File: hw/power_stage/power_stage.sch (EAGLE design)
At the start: 47 parts, among them IC1H MIC4420M, IC1L MIC4429M, IC2H MIC4420M, IC2L MIC4429M, J1 AC1, J2 AC2, J3 OUT1, J4 OUT2

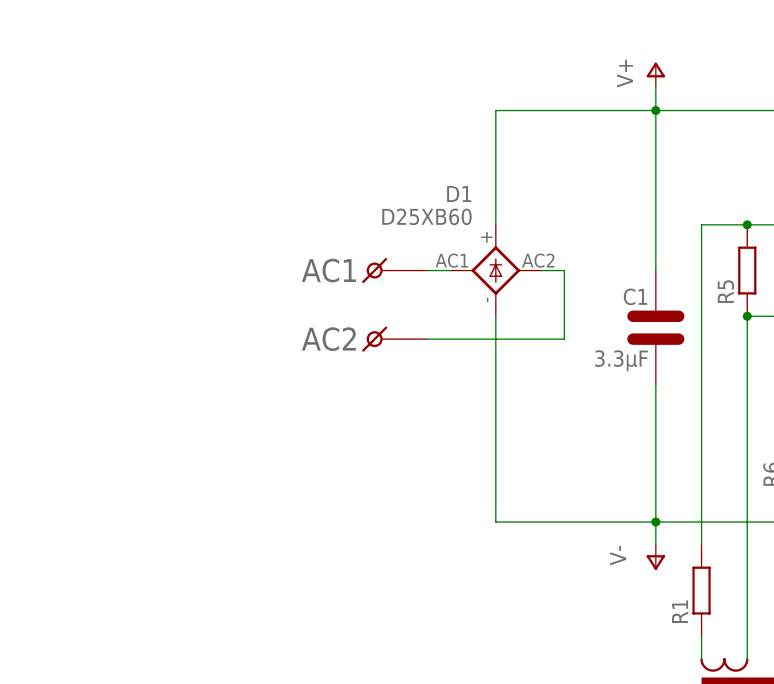
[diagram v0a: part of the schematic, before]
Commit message: Adapted power_stage.brd to be 100x100mm
This enables us to use cheap PCB fab services.
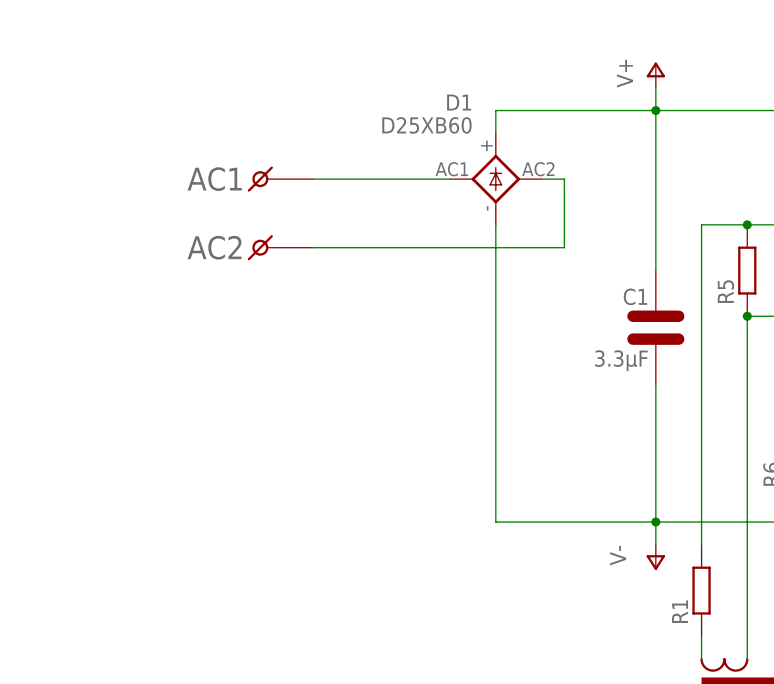
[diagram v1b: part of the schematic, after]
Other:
- moved on the sheet: D1
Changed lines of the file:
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@@
 <layer number="48" name="Document" color="7" fill="1" visible="no" active="no"/>
 <layer number="49" name="Reference" color="7" fill="1" visible="no" active="no"/>
+<layer number="50" name="dxf" color="7" fill="1" visible="no" active="no"/>
 <layer number="51" name="tDocu" color="7" fill="1" visible="no" active="no"/>
 <layer number="52" name="bDocu" color="7" fill="1" visible="no" active="no"/>
+<layer number="53" name="tGND_GNDA" color="7" fill="9" visible="no" active="no"/>
+<layer number="54" name="bGND_GNDA" color="1" fill="9" visible="no" active="no"/>
+<layer number="56" name="wert" color="7" fill="1" visible="no" active="no"/>
 <layer number="90" name="Modules" color="5" fill="1" visible="yes" active="yes"/>
 <layer number="91" name="Nets" color="2" fill="1" visible="yes" active="yes"/>
@@
 <layer number="98" name="Guide" color="6" fill="1" visible="yes" active="yes"/>
 <layer number="99" name="SpiceOrder" color="5" fill="1" visible="yes" active="yes"/>
+<layer number="100" name="Muster" color="7" fill="1" visible="no" active="no"/>
+<layer number="101" name="Patch_Top" color="12" fill="4" visible="yes" active="yes"/>
+<layer number="102" name="Vscore" color="7" fill="1" visible="yes" active="yes"/>
+<layer number="103" name="tMap" color="7" fill="1" visible="yes" active="yes"/>
+<layer number="104" name="Name" color="16" fill="1" visible="yes" active="yes"/>
+<layer number="105" name="tPlate" color="7" fill="1" visible="yes" active="yes"/>
+<layer number="106" name="bPlate" color="7" fill="1" visible="yes" active="yes"/>
+<layer number="107" name="Crop" color="7" fill="1" visible="yes" active="yes"/>
+<layer number="108" name="tplace-old" color="10" fill="1" visible="yes" active="yes"/>
+<layer number="109" name="ref-old" color="11" fill="1" visible="yes" active="yes"/>
+<layer number="116" name="Patch_BOT" color="9" fill="4" visible="yes" active="yes"/>
+<layer number="121" name="_tsilk" color="7" fill="1" visible="yes" active="yes"/>
+<layer number="122" name="_bsilk" color="7" fill="1" visible="yes" active="yes"/>
+<layer number="125" name="_tNames" color="7" fill="1" visible="yes" active="yes"/>
+<layer number="144" name="Drill_legend" color="7" fill="1" visible="yes" active="yes"/>
+<layer number="151" name="HeatSink" color="7" fill="1" visible="yes" active="yes"/>
+<layer number="199" name="Contour" color="7" fill="1" visible="yes" active="yes"/>
+<layer number="200" name="200bmp" color="1" fill="10" visible="yes" active="yes"/>
+<layer number="201" name="201bmp" color="2" fill="10" visible="yes" active="yes"/>
+<layer number="202" name="202bmp" color="3" fill="10" visible="yes" active="yes"/>
+<layer number="203" name="203bmp" color="4" fill="10" visible="yes" active="yes"/>
+<layer number="204" name="204bmp" color="5" fill="10" visible="yes" active="yes"/>
+<layer number="205" name="205bmp" color="6" fill="10" visible="yes" active="yes"/>
+<layer number="206" name="206bmp" color="7" fill="10" visible="yes" active="yes"/>
+<layer number="207" name="207bmp" color="8" fill="10" visible="yes" active="yes"/>
+<layer number="208" name="208bmp" color="9" fill="10" visible="yes" active="yes"/>
+<layer number="209" name="209bmp" color="7" fill="1" visible="yes" active="yes"/>
+<layer number="210" name="210bmp" color="7" fill="1" visible="yes" active="yes"/>
+<layer number="211" name="211bmp" color="7" fill="1" visible="yes" active="yes"/>
+<layer number="212" name="212bmp" color="7" fill="1" visible="yes" active="yes"/>
+<layer number="213" name="213bmp" color="7" fill="1" visible="yes" active="yes"/>
+<layer number="214" name="214bmp" color="7" fill="1" visible="yes" active="yes"/>
+<layer number="215" name="215bmp" color="7" fill="1" visible="yes" active="yes"/>
+<layer number="216" name="216bmp" color="7" fill="1" visible="yes" active="yes"/>
+<layer number="217" name="217bmp" color="18" fill="1" visible="no" active="no"/>
+<layer number="218" name="218bmp" color="19" fill="1" visible="no" active="no"/>
+<layer number="219" name="219bmp" color="20" fill="1" visible="no" active="no"/>
+<layer number="220" name="220bmp" color="21" fill="1" visible="no" active="no"/>
+<layer number="221" name="221bmp" color="22" fill="1" visible="no" active="no"/>
+<layer number="222" name="222bmp" color="23" fill="1" visible="no" active="no"/>
+<layer number="223" name="223bmp" color="24" fill="1" visible="no" active="no"/>
+<layer number="224" name="224bmp" color="25" fill="1" visible="no" active="no"/>
+<layer number="250" name="Descript" color="3" fill="1" visible="no" active="no"/>
+<layer number="251" name="SMDround" color="12" fill="11" visible="no" active="no"/>
+<layer number="254" name="cooling" color="7" fill="1" visible="yes" active="yes"/>
 </layers>
 <schematic xreflabel="%F%N/%S.%C%R" xrefpart="/%S.%C%R">
@@
 <attribute name="VALUE" x="-31.242" y="54.61" size="1.778" layer="96" ratio="15" align="top-right"/>
 </instance>
-<instance part="D1" gate="G$1" x="-48.26" y="63.5" smashed="yes" rot="R90">
-<attribute name="NAME" x="-50.8" y="71.12" size="1.778" layer="95" align="bottom-right"/>
-<attribute name="VALUE" x="-50.8" y="68.58" size="1.778" layer="96" align="bottom-right"/>
-</instance>
-<instance part="J1" gate="G$1" x="-60.96" y="63.5" rot="R180"/>
-<instance part="J2" gate="G$1" x="-60.96" y="55.88" rot="R180"/>
+<instance part="D1" gate="G$1" x="-48.26" y="73.66" smashed="yes" rot="R90">
+<attribute name="NAME" x="-50.8" y="81.28" size="1.778" layer="95" align="bottom-right"/>
+<attribute name="VALUE" x="-50.8" y="78.74" size="1.778" layer="96" align="bottom-right"/>
+</instance>
+<instance part="J1" gate="G$1" x="-73.66" y="73.66" rot="R180"/>
+<instance part="J2" gate="G$1" x="-73.66" y="66.04" rot="R180"/>
 <instance part="IGBT1H" gate="G$1" x="-2.54" y="71.12" smashed="yes">
 <attribute name="NAME" x="-5.08" y="69.596" size="1.778" layer="95" align="bottom-right"/>
@@
 <net name="AC2" class="0">
 <segment>
-<wire x1="-40.64" y1="55.88" x2="-40.64" y2="63.5" width="0.1524" layer="91"/>
+<wire x1="-40.64" y1="66.04" x2="-40.64" y2="73.66" width="0.1524" layer="91"/>
 <pinref part="D1" gate="G$1" pin="AC2"/>
-<wire x1="-40.64" y1="63.5" x2="-43.18" y2="63.5" width="0.1524" layer="91"/>
+<wire x1="-40.64" y1="73.66" x2="-43.18" y2="73.66" width="0.1524" layer="91"/>
 <pinref part="J2" gate="G$1" pin="1"/>
-<wire x1="-55.88" y1="55.88" x2="-40.64" y2="55.88" width="0.1524" layer="91"/>
+<wire x1="-68.58" y1="66.04" x2="-40.64" y2="66.04" width="0.1524" layer="91"/>
 </segment>
 </net>
@@
 <pinref part="D1" gate="G$1" pin="AC1"/>
 <pinref part="J1" gate="G$1" pin="1"/>
-<wire x1="-53.34" y1="63.5" x2="-55.88" y2="63.5" width="0.1524" layer="91"/>
+<wire x1="-53.34" y1="73.66" x2="-68.58" y2="73.66" width="0.1524" layer="91"/>
 </segment>
 </net>
@@
 <segment>
 <pinref part="D1" gate="G$1" pin="-"/>
-<wire x1="-48.26" y1="58.42" x2="-48.26" y2="35.56" width="0.1524" layer="91"/>
+<wire x1="-48.26" y1="68.58" x2="-48.26" y2="35.56" width="0.1524" layer="91"/>
 <wire x1="-48.26" y1="35.56" x2="-30.48" y2="35.56" width="0.1524" layer="91"/>
 <pinref part="IGBT1L" gate="G$1" pin="E"/>
@@
 <pinref part="D1" gate="G$1" pin="+"/>
 <wire x1="-30.48" y1="81.28" x2="-48.26" y2="81.28" width="0.1524" layer="91"/>
-<wire x1="-48.26" y1="81.28" x2="-48.26" y2="68.58" width="0.1524" layer="91"/>
+<wire x1="-48.26" y1="81.28" x2="-48.26" y2="78.74" width="0.1524" layer="91"/>
 <junction x="0" y="81.28"/>
 <pinref part="C1" gate="G$1" pin="P$2"/>

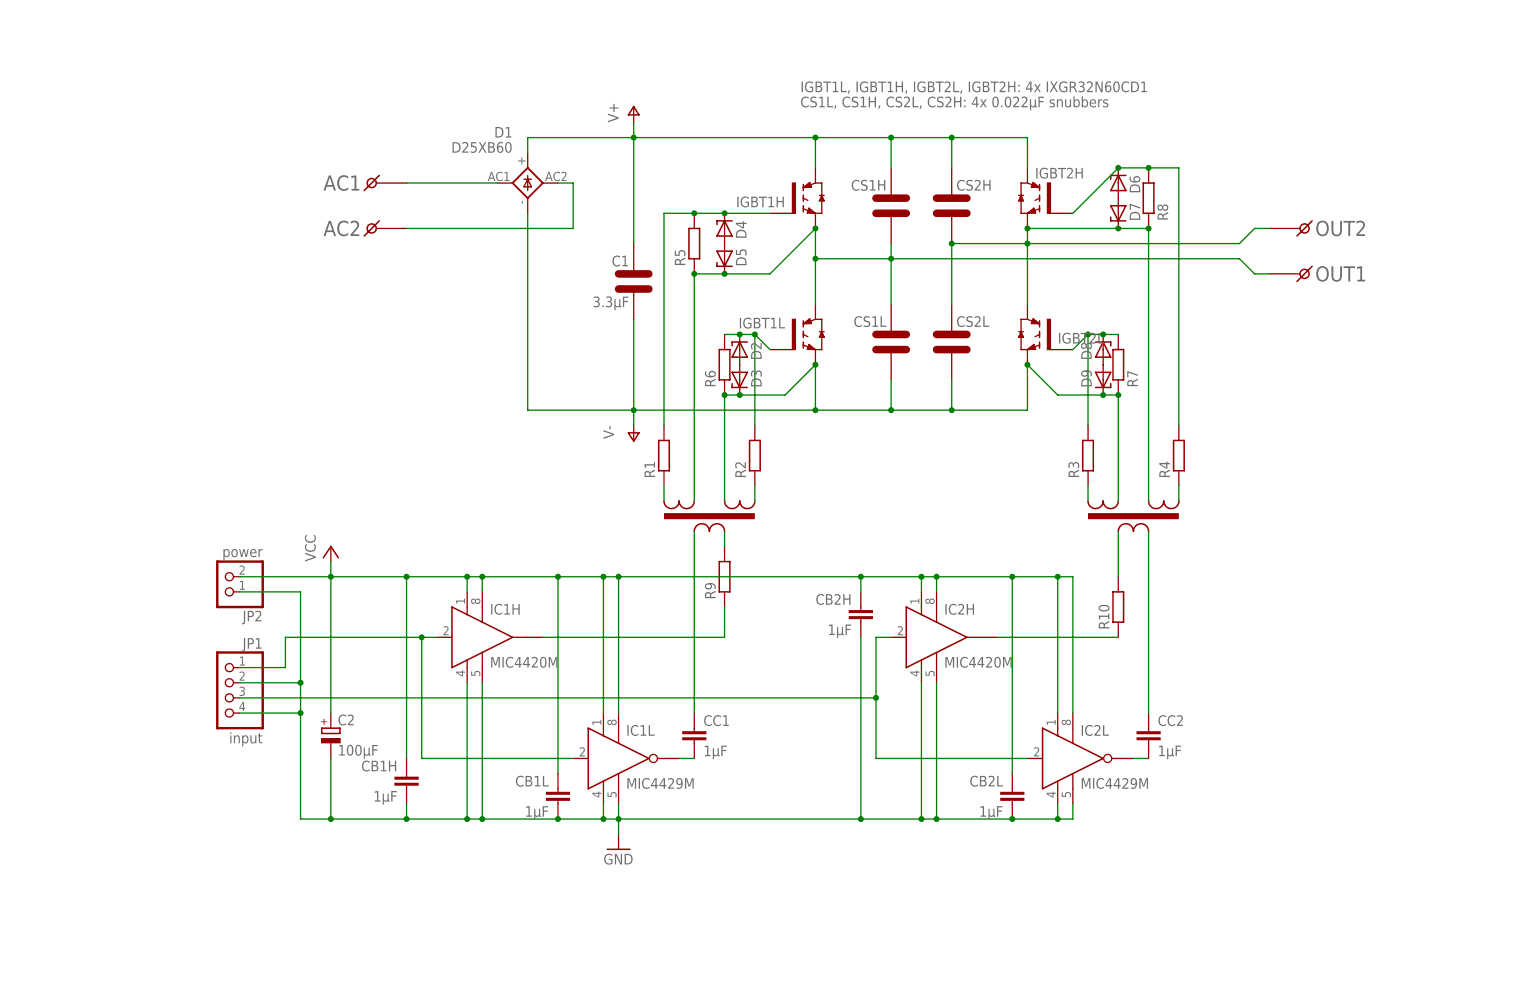
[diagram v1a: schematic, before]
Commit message: Remove solder mask from high current tracks so we can cheaply increase their current capacity
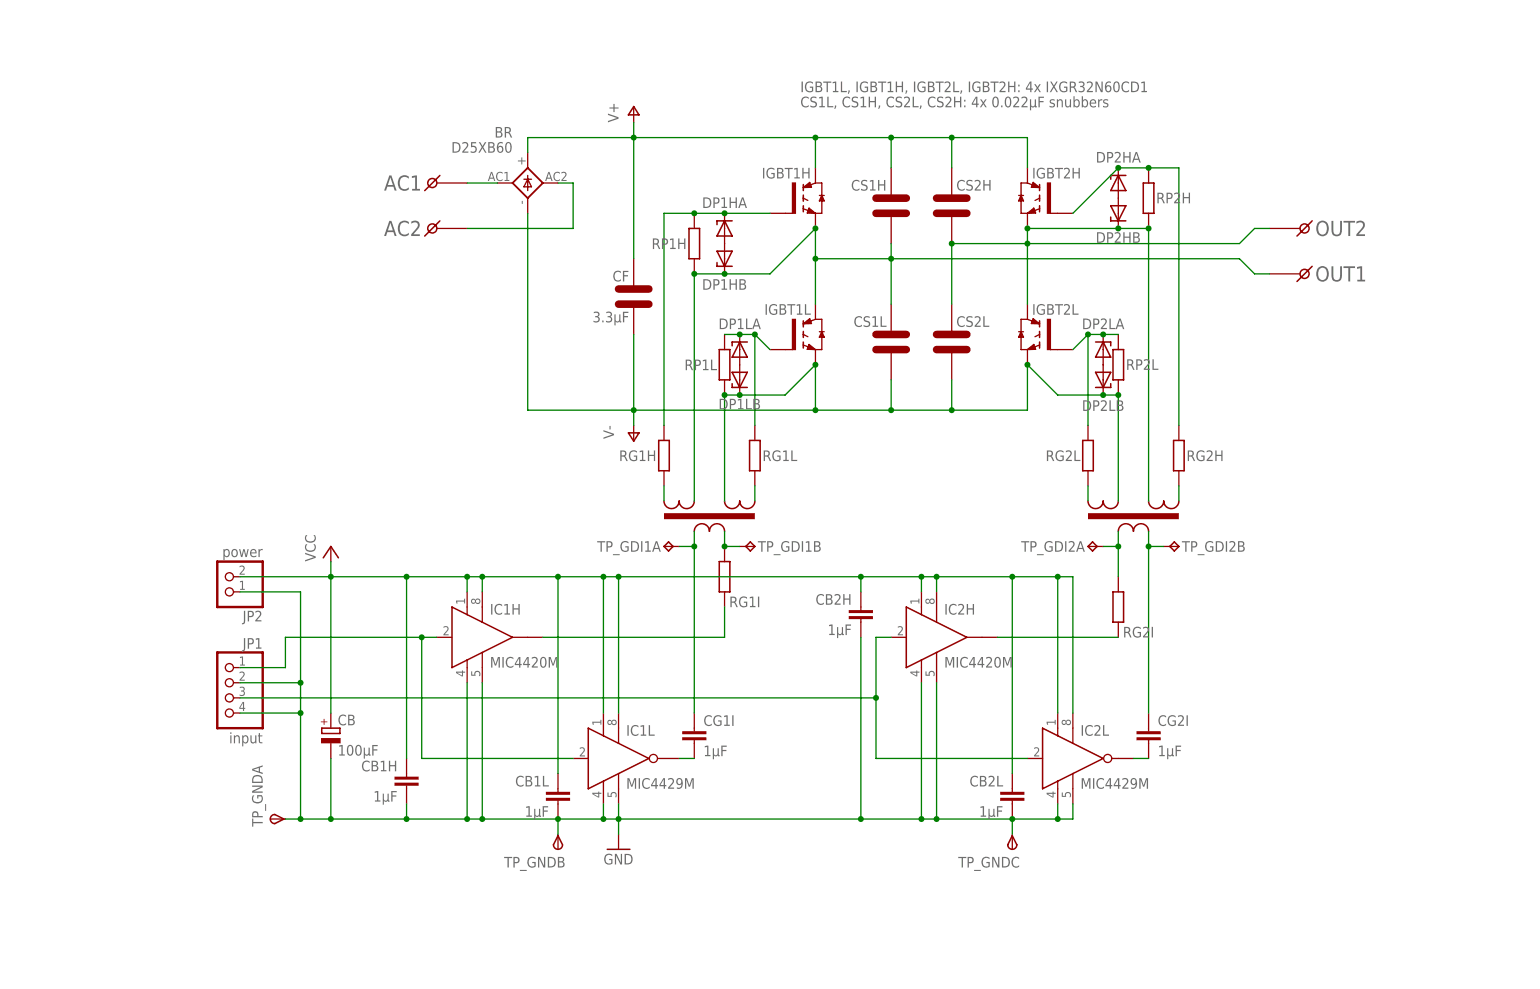
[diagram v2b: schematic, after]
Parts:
- removed C1: 3.3µF, induction-heater:C_R75
- removed J1: AC1, induction-heater:SCREW
- removed J2: AC2, induction-heater:SCREW
- added AC1: AC1, induction-heater:SCREW
- added AC2: AC2, induction-heater:SCREW
- added CF: 3.3µF, induction-heater:C_R75
- added TP_GDI1A, TP_GDI2B: A, testpad:TPTP10SQ
- added TP_GDI1B, TP_GDI2A: B, testpad:TPTP10SQ
- added TP_GNDA, TP_GNDB, TP_GNDC: GND, testpad:TPSPAD1-13
- renumbered C2 to CB, CC1 to CG1I, CC2 to CG2I, D1 to BR, D2 to DP1LA, D3 to DP1LB, D4 to DP1HA, D5 to DP1HB, D6 to DP2HA, D7 to DP2HB, D8 to DP2LA, D9 to DP2LB, J3 to OUT1, J4 to OUT2, R1 to RG1H, R10 to RG2I, R2 to RG1L, R3 to RG2L, R4 to RG2H, R5 to RP1H, R6 to RP1L, R7 to RP2L, R8 to RP2H, R9 to RG1I
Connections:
- net AC1: now also AC1.1; no longer J1.1
- net AC2: now also AC2.1; no longer J2.1
- net GND: now also TP_GNDA.PP, TP_GNDB.PP, TP_GNDC.PP
- net N$1: now also TP_GDI1B.TP
- net N$26: now also TP_GDI1A.TP
- net N$27: now also TP_GDI2B.TP
- net N$5: now also TP_GDI2A.TP
- net V+: now also CF.P$2; no longer C1.P$2
- net V-: now also CF.P$1; no longer C1.P$1

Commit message: More fiddling
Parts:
- JP1: value input -> control
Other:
- note added: "IGBT[12][HL]: 4x IXGR32N60CD1 IXYS IGBTs CS[12][HL]: 4x 0.022µF KEMET R76 snubbers CF: 3.3µF KEMET R75 filter cap DP[12][HL][AB]: 8x 20V zener for protection RP[12][HL]: 4x +/- 10kohm RG[12][HL]: 4x +/- 47ohm"
- note removed: "CS1L, CS1H, CS2L, CS2H: 4x 0.022µF snubbers"
- note removed: "IGBT1L, IGBT1H, IGBT2L, IGBT2H: 4x IXGR32N60CD1"
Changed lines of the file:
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@@
 <part name="CB2L" library="rcl" deviceset="C-EU" device="C0805" value="1µF"/>
 <part name="CB2H" library="rcl" deviceset="C-EU" device="C0805" value="1µF"/>
-<part name="JP1" library="pinhead" deviceset="PINHD-1X4" device="" value="input"/>
+<part name="JP1" library="pinhead" deviceset="PINHD-1X4" device="" value="control"/>
 <part name="JP2" library="pinhead" deviceset="PINHD-1X2" device="" value="power"/>
 <part name="CB" library="rcl" deviceset="CPOL-EU" device="E2.5-7" value="100µF"/>
@@
 <sheet>
 <plain>
-<text x="-2.54" y="86.36" size="1.778" layer="96">CS1L, CS1H, CS2L, CS2H: 4x 0.022µF snubbers</text>
-<text x="-2.54" y="88.9" size="1.778" layer="96">IGBT1L, IGBT1H, IGBT2L, IGBT2H: 4x IXGR32N60CD1</text>
+<text x="-5.08" y="86.36" size="1.778" layer="96">IGBT[12][HL]: 4x IXGR32N60CD1 IXYS IGBTs
+CS[12][HL]: 4x 0.022µF KEMET R76 snubbers
+CF: 3.3µF KEMET R75 filter cap
+DP[12][HL][AB]: 8x 20V zener for protection
+RP[12][HL]: 4x +/- 10kohm
+RG[12][HL]: 4x +/- 47ohm</text>
 </plain>
 <instances>
@@
 </schematic>
 </drawing>
+<compatibility>
+<note version="6.3" minversion="6.2.2" severity="warning">
+Since Version 6.2.2 text objects can contain more than one line,
+which will not be processed correctly with this version.
+</note>
+</compatibility>
 </eagle>
